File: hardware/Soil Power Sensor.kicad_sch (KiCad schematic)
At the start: 0 parts

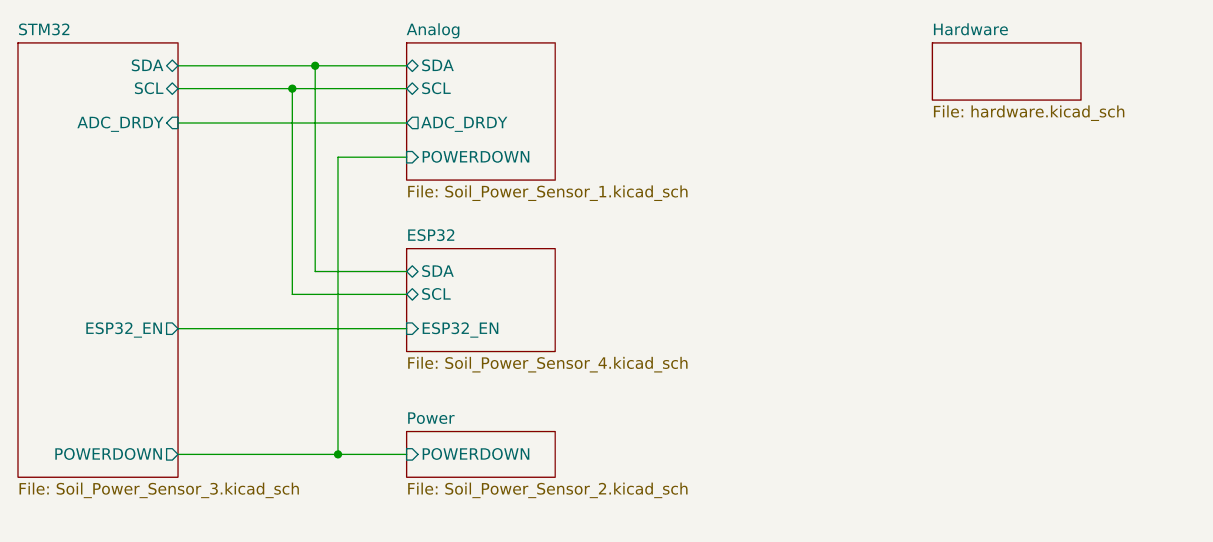
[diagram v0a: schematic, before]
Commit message: Added wakeup line for esp32
Closes #48
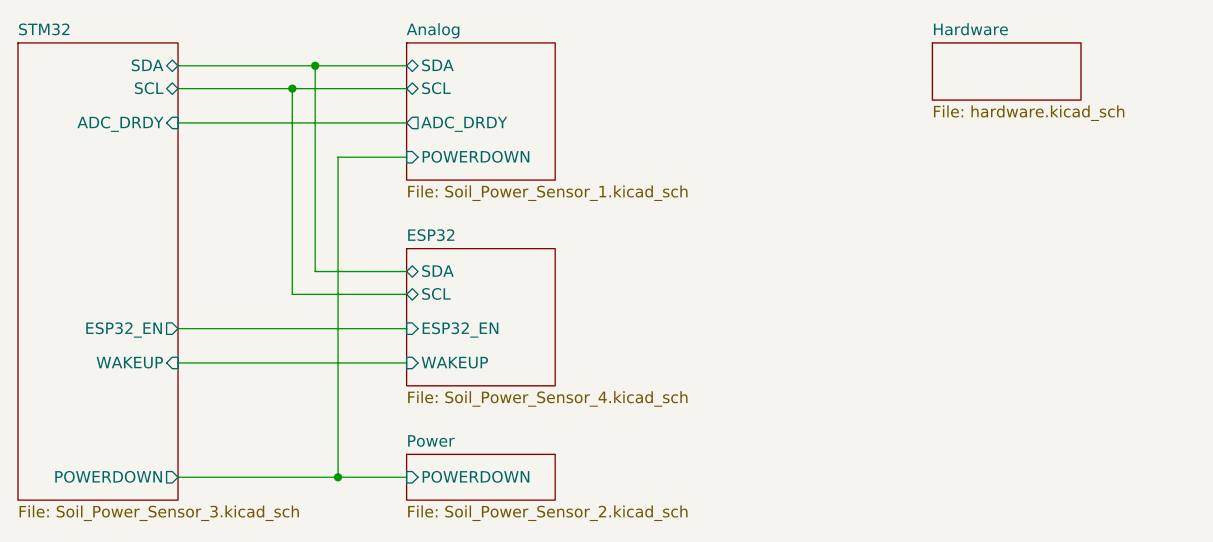
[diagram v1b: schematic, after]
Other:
- sheet ESP32 ports: added WAKEUP; removed none
- sheet STM32 ports: added WAKEUP; removed none
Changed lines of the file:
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@@
-	)
-	(junction
-		(at 154.94 118.11)
-		(diameter 0)
-		(color 0 0 0 0)
 	)
 	(junction
@@
 		(color 0 0 0 0)
 	)
+	(junction
+		(at 154.94 120.65)
+		(diameter 0)
+		(color 0 0 0 0)
+	)
 	(wire
 		(pts
@@
 	(wire
 		(pts
+			(xy 137.16 107.95) (xy 162.56 107.95)
+		)
+		(stroke
+			(width 0)
+			(type default)
+		)
+	)
+	(wire
+		(pts
 			(xy 162.56 100.33) (xy 149.86 100.33)
 		)
@@
 	(wire
 		(pts
+			(xy 154.94 85.09) (xy 154.94 120.65)
+		)
+		(stroke
+			(width 0)
+			(type default)
+		)
+	)
+	(wire
+		(pts
 			(xy 152.4 74.93) (xy 162.56 74.93)
 		)
@@
 	(wire
 		(pts
-			(xy 154.94 85.09) (xy 154.94 118.11)
-		)
-		(stroke
-			(width 0)
-			(type default)
-		)
-	)
-	(wire
-		(pts
 			(xy 137.16 77.47) (xy 149.86 77.47)
 		)
@@
 	(wire
 		(pts
-			(xy 154.94 118.11) (xy 162.56 118.11)
+			(xy 154.94 120.65) (xy 162.56 120.65)
 		)
 		(stroke
@@
 	(wire
 		(pts
-			(xy 137.16 118.11) (xy 154.94 118.11)
+			(xy 137.16 120.65) (xy 154.94 120.65)
 		)
 		(stroke
@@
 	(sheet
 		(at 162.56 95.25)
-		(size 16.51 11.43)
+		(size 16.51 15.24)
 		(fields_autoplaced yes)
 		(stroke
@@
 		)
 		(property "Sheetfile" "Soil_Power_Sensor_4.kicad_sch"
-			(at 162.56 107.2646 0)
+			(at 162.56 111.0746 0)
 			(effects
 				(font
@@
 		(pin "SDA" bidirectional
 			(at 162.56 97.79 180)
+			(effects
+				(font
+					(size 1.27 1.27)
+				)
+				(justify left)
+			)
+		)
+		(pin "WAKEUP" input
+			(at 162.56 107.95 180)
 			(effects
 				(font
@@
 	(sheet
 		(at 119.38 72.39)
-		(size 17.78 48.26)
+		(size 17.78 50.8)
 		(fields_autoplaced yes)
 		(stroke
@@
 		)
 		(property "Sheetfile" "Soil_Power_Sensor_3.kicad_sch"
-			(at 119.38 121.2346 0)
+			(at 119.38 123.7746 0)
 			(effects
 				(font
@@
 		)
 		(pin "POWERDOWN" output
-			(at 137.16 118.11 0)
+			(at 137.16 120.65 0)
+			(effects
+				(font
+					(size 1.27 1.27)
+				)
+				(justify right)
+			)
+		)
+		(pin "WAKEUP" input
+			(at 137.16 107.95 0)
 			(effects
 				(font
@@
 	)
 	(sheet
-		(at 162.56 115.57)
+		(at 162.56 118.11)
 		(size 16.51 5.08)
 		(fields_autoplaced yes)
@@
 		)
 		(property "Sheetname" "Power"
-			(at 162.56 114.8584 0)
+			(at 162.56 117.3984 0)
 			(effects
 				(font
@@
 		)
 		(property "Sheetfile" "Soil_Power_Sensor_2.kicad_sch"
-			(at 162.56 121.2346 0)
+			(at 162.56 123.7746 0)
 			(effects
 				(font
@@
 		)
 		(pin "POWERDOWN" input
-			(at 162.56 118.11 180)
-			(effects
-				(font
+			(at 162.56 120.65 180)
+			(effects
+				(font
